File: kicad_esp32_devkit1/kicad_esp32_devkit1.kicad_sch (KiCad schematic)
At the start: 30 parts

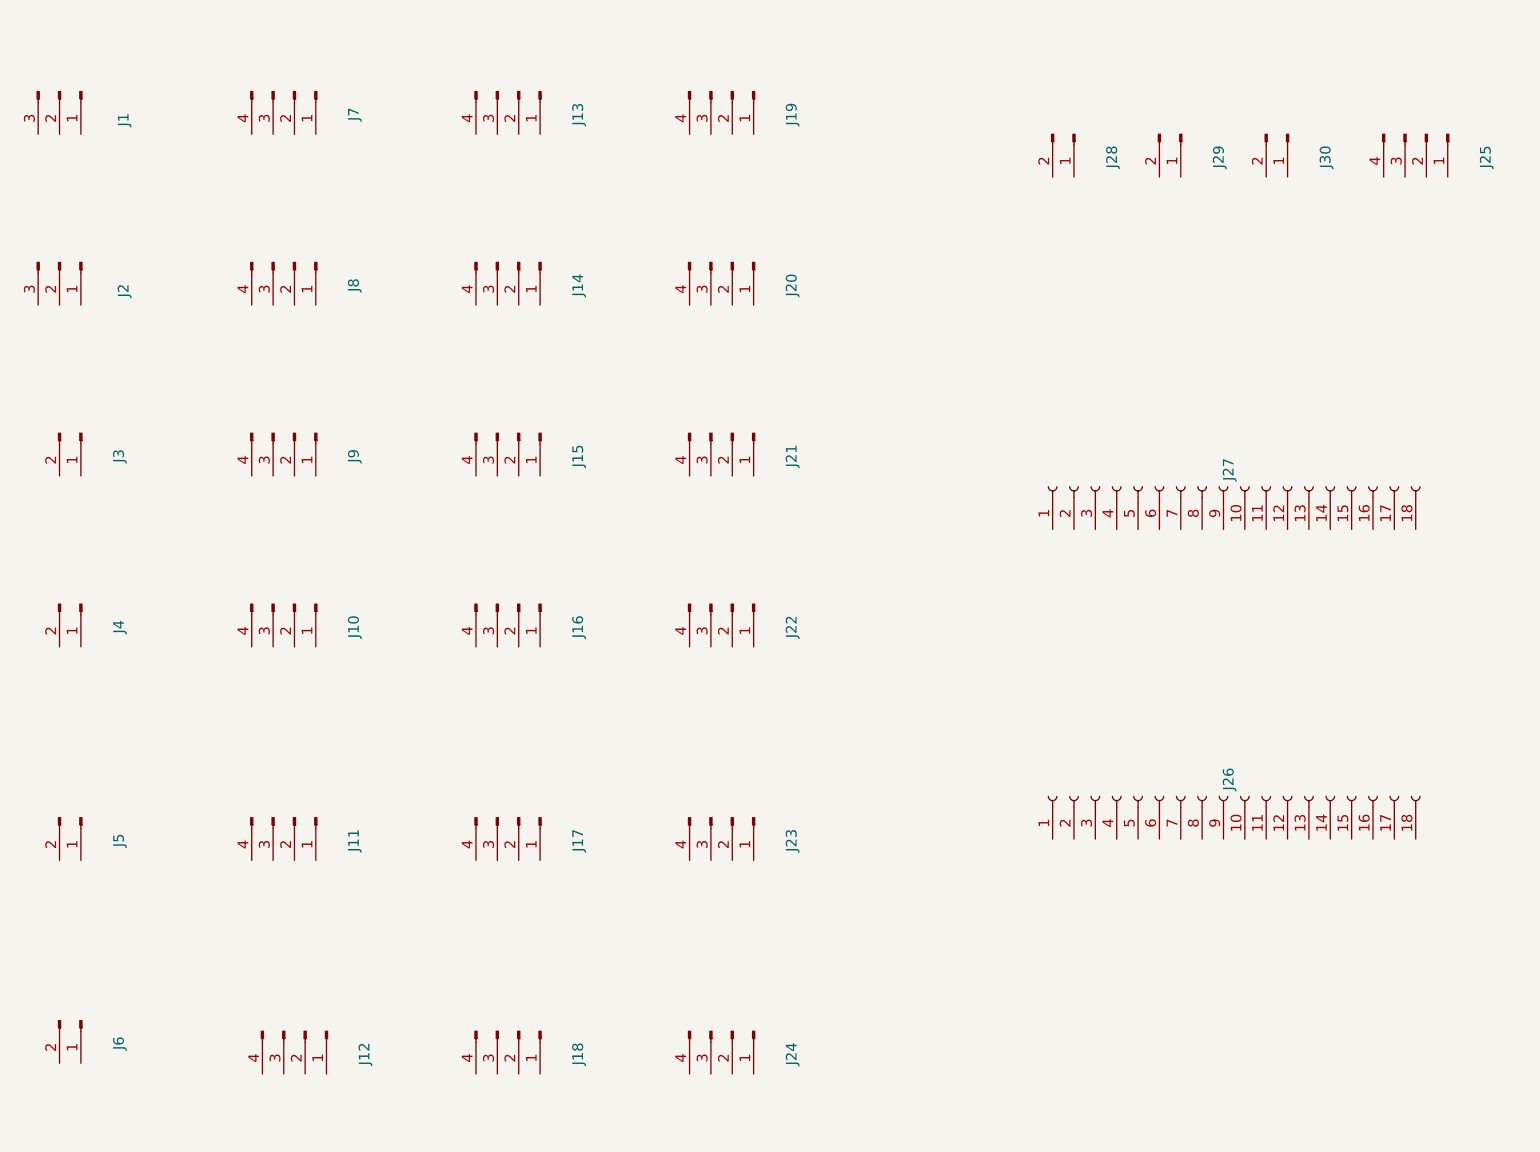
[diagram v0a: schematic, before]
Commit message: Connecting the pins
Add the first few connections.
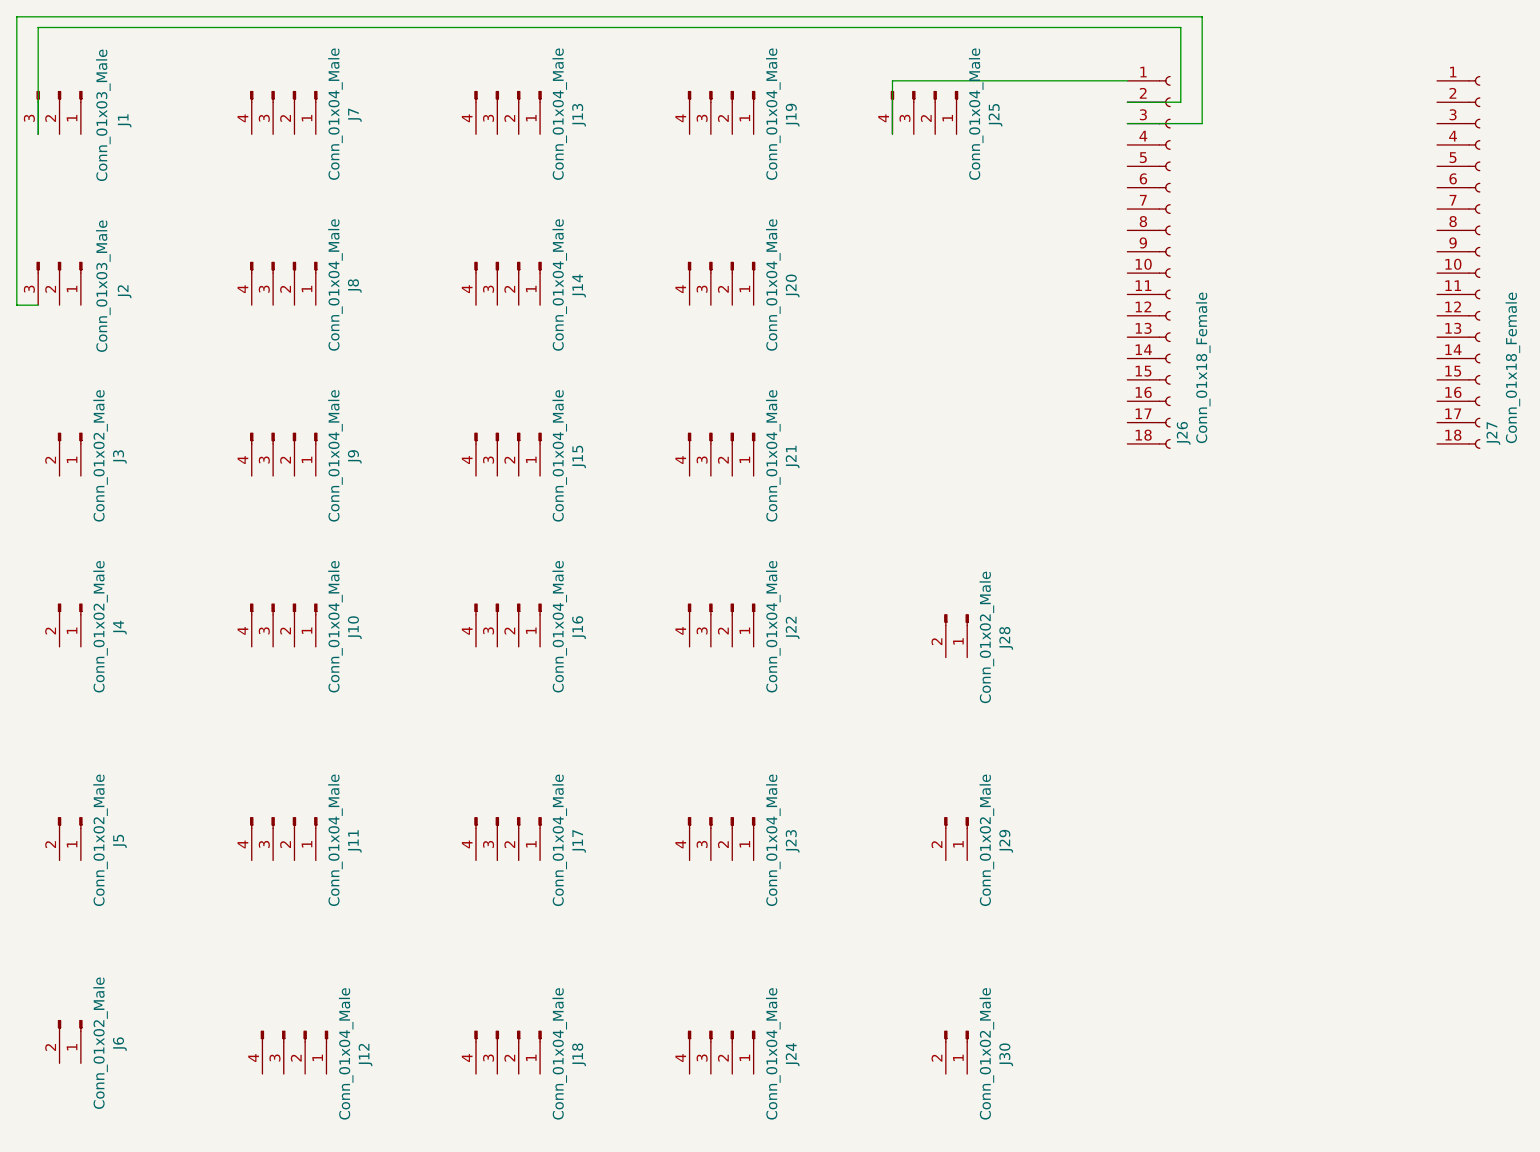
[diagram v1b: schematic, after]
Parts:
- J1, J2: value (none) -> Conn_01x03_Male; footprint (none) -> Connector_Molex:Molex_KK-254_AE-6410-03A_1x03_P2.54mm_Vertical
- J10, J11, J12, J13, J14, J15, J16, J17, J18, J19, J20, J21, J22, J23, J24, J25, J7, J8, J9: value (none) -> Conn_01x04_Male; footprint (none) -> Connector_Molex:Molex_KK-254_AE-6410-04A_1x04_P2.54mm_Vertical
- J26, J27: value (none) -> Conn_01x18_Female; footprint (none) -> Connector_PinHeader_2.54mm:PinHeader_1x18_P2.54mm_Vertical
- J28, J29, J3, J30, J4, J5, J6: value (none) -> Conn_01x02_Male; footprint (none) -> Connector_Molex:Molex_KK-254_AE-6410-02A_1x02_P2.54mm_Vertical
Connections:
- net at J2.3 (Pin_3): now also J26.3 (Pin_3)
- net at J1.3 (Pin_3): now also J26.2 (Pin_2)
- net at J25.4 (Pin_4): now also J26.1 (Pin_1)
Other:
- moved on the sheet: J25, J26, J27, J28, J29, J30
